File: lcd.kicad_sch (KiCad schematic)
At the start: 3 parts

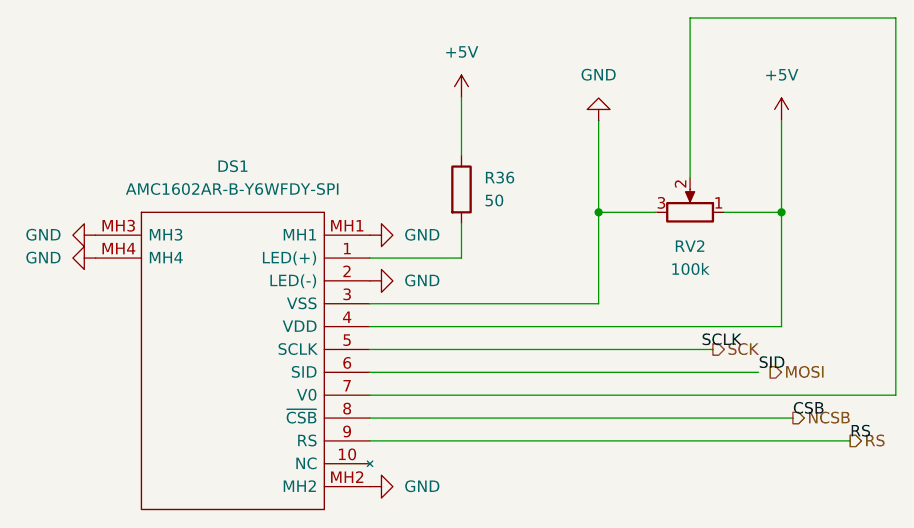
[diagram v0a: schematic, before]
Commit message: Routing of some wires
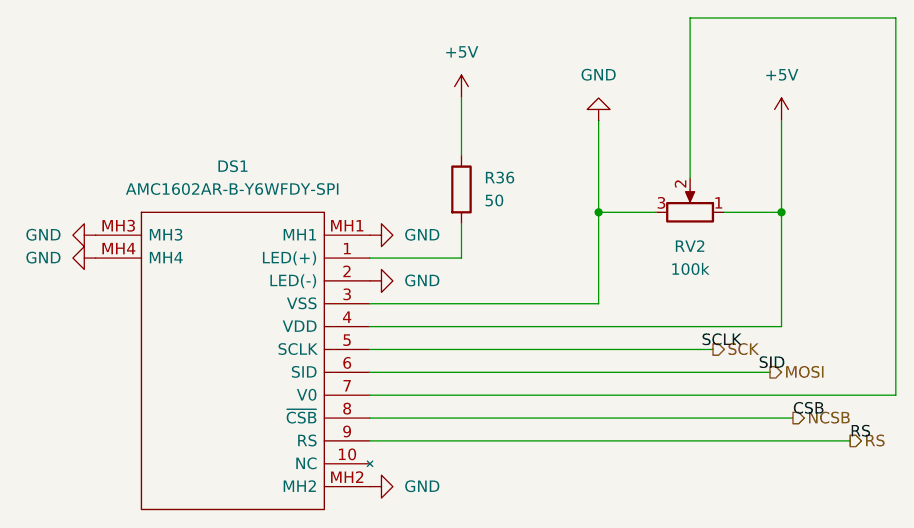
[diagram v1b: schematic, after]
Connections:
- net SID is gone; now on net MOSI: DS1.6 (SID)
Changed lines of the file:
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@@
     (stroke (width 0) (type default) (color 0 0 0 0))
   )
-  (wire (pts (xy 120.65 90.17) (xy 163.83 90.17))
+  (wire (pts (xy 120.65 90.17) (xy 165.1 90.17))
     (stroke (width 0) (type default) (color 0 0 0 0))
   )

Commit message: First week after winter break. Changed Power circuit design to use different DC to DC converter Setting correct footprints for the components like resistors and capacitors.
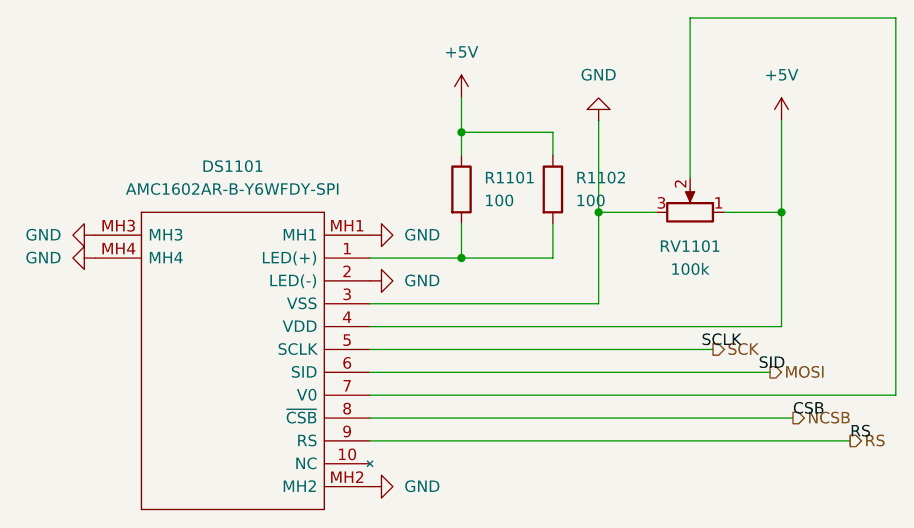
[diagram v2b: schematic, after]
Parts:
- added R1102: 100, Resistor_SMD:R_0603_1608Metric, symbol Device:R
- R1101: renamed from R36; value 50 -> 100; footprint Resistor_SMD:R_0201_0603Metric -> Resistor_SMD:R_0603_1608Metric; Manufacturer_Name (none) -> UNI-ROYAL(Uniroyal Elec); Manufacturer_Part_Number (none) -> 0603WAF1000T5E
- renumbered DS1 to DS1101, RV2 to RV1101
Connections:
- net +5V: now also R1102.1
- net at DS1101.1 (LED(+)), R1101.2: now also R1102.2
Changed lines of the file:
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@@
   (junction (at 146.05 72.39) (diameter 0) (color 0 0 0 0)
   )
+  (junction (at 130.81 63.5) (diameter 0) (color 0 0 0 0)
+  )
+  (junction (at 130.81 77.47) (diameter 0) (color 0 0 0 0)
+  )
   (junction (at 166.37 72.39) (diameter 0) (color 0 0 0 0)
   )
@@
     (stroke (width 0) (type default) (color 0 0 0 0))
   )
+  (wire (pts (xy 130.81 63.5) (xy 140.97 63.5))
+    (stroke (width 0) (type default) (color 0 0 0 0))
+  )
   (wire (pts (xy 120.65 92.71) (xy 179.07 92.71))
     (stroke (width 0) (type default) (color 0 0 0 0))
@@
     (stroke (width 0) (type default) (color 0 0 0 0))
   )
+  (wire (pts (xy 130.81 63.5) (xy 130.81 66.04))
+    (stroke (width 0) (type default) (color 0 0 0 0))
+  )
   (wire (pts (xy 120.65 85.09) (xy 166.37 85.09))
     (stroke (width 0) (type default) (color 0 0 0 0))
@@
     (stroke (width 0) (type default) (color 0 0 0 0))
   )
-  (wire (pts (xy 130.81 59.69) (xy 130.81 66.04))
+  (wire (pts (xy 140.97 66.04) (xy 140.97 63.5))
+    (stroke (width 0) (type default) (color 0 0 0 0))
+  )
+  (wire (pts (xy 130.81 59.69) (xy 130.81 63.5))
     (stroke (width 0) (type default) (color 0 0 0 0))
   )
@@
     (stroke (width 0) (type default) (color 0 0 0 0))
   )
+  (wire (pts (xy 130.81 77.47) (xy 140.97 77.47))
+    (stroke (width 0) (type default) (color 0 0 0 0))
+  )
   (wire (pts (xy 146.05 72.39) (xy 146.05 82.55))
     (stroke (width 0) (type default) (color 0 0 0 0))
   )
   (wire (pts (xy 156.21 50.8) (xy 156.21 68.58))
+    (stroke (width 0) (type default) (color 0 0 0 0))
+  )
+  (wire (pts (xy 140.97 73.66) (xy 140.97 77.47))
     (stroke (width 0) (type default) (color 0 0 0 0))
   )
@@
   (symbol (lib_id "power:GND") (at 120.65 102.87 90) (unit 1)
     (in_bom yes) (on_board yes) (fields_autoplaced)
-    (property "Reference" "#PWR0150" (id 0) (at 127 102.87 0)
+    (property "Reference" "#PWR01105" (id 0) (at 127 102.87 0)
       (effects (font (size 1.27 1.27)) hide)
     )
@@
   (symbol (lib_id "AMC1602AR-B-Y6WFDY-SPI:AMC1602AR-B-Y6WFDY-SPI") (at 90.17 74.93 0) (unit 1)
     (in_bom yes) (on_board yes) (fields_autoplaced)
-    (property "Reference" "DS1" (id 0) (at 105.41 67.31 0))
+    (property "Reference" "DS1101" (id 0) (at 105.41 67.31 0))
     (property "Value" "AMC1602AR-B-Y6WFDY-SPI" (id 1) (at 105.41 69.85 0))
     (property "Footprint" "Custom:AMC1602ARBY6WFDYSPI" (id 2) (at 116.84 72.39 0)
@@
   (symbol (lib_id "Device:R_Potentiometer") (at 156.21 72.39 270) (mirror x) (unit 1)
     (in_bom yes) (on_board yes) (fields_autoplaced)
-    (property "Reference" "RV2" (id 0) (at 156.21 76.2 90))
+    (property "Reference" "RV1101" (id 0) (at 156.21 76.2 90))
     (property "Value" "100k" (id 1) (at 156.21 78.74 90))
     (property "Footprint" "Custom:TRIM_3352T-1-104LF" (id 2) (at 156.21 72.39 0)
@@
   (symbol (lib_id "power:GND") (at 120.65 80.01 90) (unit 1)
     (in_bom yes) (on_board yes) (fields_autoplaced)
-    (property "Reference" "#PWR0151" (id 0) (at 127 80.01 0)
+    (property "Reference" "#PWR01104" (id 0) (at 127 80.01 0)
       (effects (font (size 1.27 1.27)) hide)
     )
@@
   (symbol (lib_id "power:GND") (at 120.65 74.93 90) (unit 1)
     (in_bom yes) (on_board yes) (fields_autoplaced)
-    (property "Reference" "#PWR0148" (id 0) (at 127 74.93 0)
+    (property "Reference" "#PWR01103" (id 0) (at 127 74.93 0)
       (effects (font (size 1.27 1.27)) hide)
     )
@@
     (pin "1")
   )
+  (symbol (lib_id "Device:R") (at 140.97 69.85 0) (unit 1)
+    (in_bom yes) (on_board yes) (fields_autoplaced)
+    (property "Reference" "R1102" (id 0) (at 143.51 68.5799 0)
+      (effects (font (size 1.27 1.27)) (justify left))
+    )
+    (property "Value" "100" (id 1) (at 143.51 71.1199 0)
+      (effects (font (size 1.27 1.27)) (justify left))
+    )
+    (property "Footprint" "Resistor_SMD:R_0603_1608Metric" (id 2) (at 139.192 69.85 90)
+      (effects (font (size 1.27 1.27)) hide)
+    )
+    (property "Datasheet" "~" (id 3) (at 140.97 69.85 0)
+      (effects (font (size 1.27 1.27)) hide)
+    )
+    (property "Manufacturer_Name" "UNI-ROYAL(Uniroyal Elec)" (id 4) (at 140.97 69.85 0)
+      (effects (font (size 1.27 1.27)) hide)
+    )
+    (property "Manufacturer_Part_Number" "0603WAF1000T5E" (id 5) (at 140.97 69.85 0)
+      (effects (font (size 1.27 1.27)) hide)
+    )
+    (pin "1")
+    (pin "2")
+  )
   (symbol (lib_id "power:GND") (at 90.17 74.93 270) (unit 1)
     (in_bom yes) (on_board yes) (fields_autoplaced)
-    (property "Reference" "#PWR0153" (id 0) (at 83.82 74.93 0)
+    (property "Reference" "#PWR01101" (id 0) (at 83.82 74.93 0)
       (effects (font (size 1.27 1.27)) hide)
     )
@@
   (symbol (lib_id "power:+5V") (at 130.81 59.69 0) (unit 1)
     (in_bom yes) (on_board yes) (fields_autoplaced)
-    (property "Reference" "#PWR0146" (id 0) (at 130.81 63.5 0)
+    (property "Reference" "#PWR01106" (id 0) (at 130.81 63.5 0)
       (effects (font (size 1.27 1.27)) hide)
     )
@@
   (symbol (lib_id "power:+5V") (at 166.37 62.23 0) (unit 1)
     (in_bom yes) (on_board yes) (fields_autoplaced)
-    (property "Reference" "#PWR0149" (id 0) (at 166.37 66.04 0)
+    (property "Reference" "#PWR01108" (id 0) (at 166.37 66.04 0)
       (effects (font (size 1.27 1.27)) hide)
     )
@@
   (symbol (lib_id "power:GND") (at 146.05 62.23 180) (unit 1)
     (in_bom yes) (on_board yes) (fields_autoplaced)
-    (property "Reference" "#PWR0147" (id 0) (at 146.05 55.88 0)
+    (property "Reference" "#PWR01107" (id 0) (at 146.05 55.88 0)
       (effects (font (size 1.27 1.27)) hide)
     )
@@
   (symbol (lib_id "power:GND") (at 90.17 77.47 270) (unit 1)
     (in_bom yes) (on_board yes) (fields_autoplaced)
-    (property "Reference" "#PWR0152" (id 0) (at 83.82 77.47 0)
+    (property "Reference" "#PWR01102" (id 0) (at 83.82 77.47 0)
       (effects (font (size 1.27 1.27)) hide)
     )
@@
   (symbol (lib_id "Device:R") (at 130.81 69.85 0) (unit 1)
     (in_bom yes) (on_board yes) (fields_autoplaced)
-    (property "Reference" "R36" (id 0) (at 133.35 68.5799 0)
+    (property "Reference" "R1101" (id 0) (at 133.35 68.5799 0)
       (effects (font (size 1.27 1.27)) (justify left))
     )
-    (property "Value" "50" (id 1) (at 133.35 71.1199 0)
+    (property "Value" "100" (id 1) (at 133.35 71.1199 0)
       (effects (font (size 1.27 1.27)) (justify left))
     )
-    (property "Footprint" "Resistor_SMD:R_0201_0603Metric" (id 2) (at 129.032 69.85 90)
+    (property "Footprint" "Resistor_SMD:R_0603_1608Metric" (id 2) (at 129.032 69.85 90)
       (effects (font (size 1.27 1.27)) hide)
     )
@@
       (effects (font (size 1.27 1.27)) hide)
     )
+    (property "Manufacturer_Name" "UNI-ROYAL(Uniroyal Elec)" (id 4) (at 130.81 69.85 0)
+      (effects (font (size 1.27 1.27)) hide)
+    )
+    (property "Manufacturer_Part_Number" "0603WAF1000T5E" (id 5) (at 130.81 69.85 0)
+      (effects (font (size 1.27 1.27)) hide)
+    )

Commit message: Weekend progress
Things that remain:
4 LEDs to Microcontroller
7-Seg to Microcontroller
LCD to Microcontroller
Microphone and Speakers to Microcontroller
Power circuitry
USB-C connector
Reset and Boot buttons
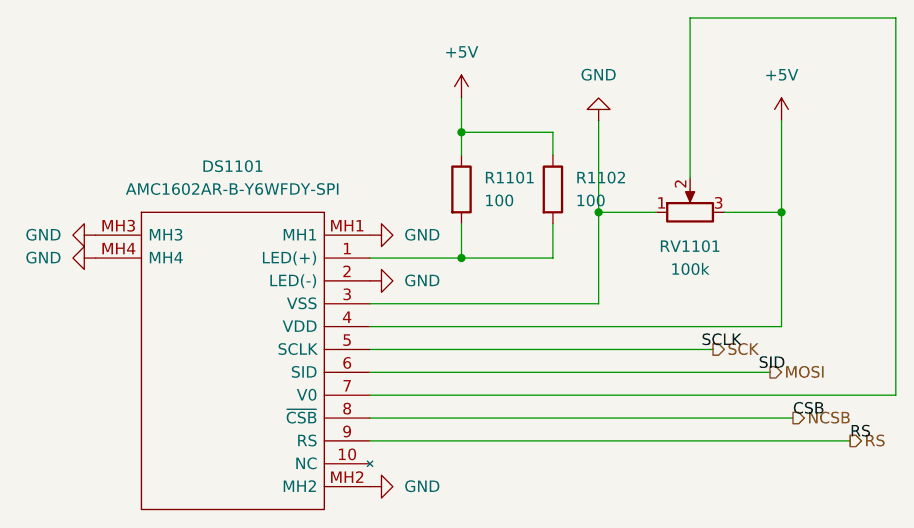
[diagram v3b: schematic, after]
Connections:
- net +5V: now also RV1101.3; no longer RV1101.1
- net GND: now also RV1101.1; no longer RV1101.3
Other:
- moved on the sheet: RV1101
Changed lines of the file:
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@@
     (pin "MH4")
   )
-  (symbol (lib_id "Device:R_Potentiometer") (at 156.21 72.39 270) (mirror x) (unit 1)
+  (symbol (lib_id "Device:R_Potentiometer") (at 156.21 72.39 90) (unit 1)
     (in_bom yes) (on_board yes) (fields_autoplaced)
     (property "Reference" "RV1101" (id 0) (at 156.21 76.2 90))

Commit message: Update BOM and POC files
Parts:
- RV1101: Manufacturer_Name (none) -> Bourns Inc.; Manufacturer_Part_Number (none) -> 3352T-1-104LF
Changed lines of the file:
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@@
+      (effects (font (size 1.27 1.27)) hide)
+    )
+    (property "Manufacturer_Name" "Bourns Inc." (id 4) (at 156.21 72.39 0)
+      (effects (font (size 1.27 1.27)) hide)
+    )
+    (property "Manufacturer_Part_Number" "3352T-1-104LF" (id 5) (at 156.21 72.39 0)
       (effects (font (size 1.27 1.27)) hide)
     )
